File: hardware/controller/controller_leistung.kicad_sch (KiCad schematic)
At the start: 51 parts, among them J1 230V~, J2 LOAD, Q1 AO3401A, Q2 BSS138, Q3 IRLML6346, Q4 IRLML6346, Q5 IRLML6346, U1 IRM-10-5, U2 AP7361C-33E, U7 SN74LVC74AD, U8 TPS3828-33DBV, U9 TC6501P065

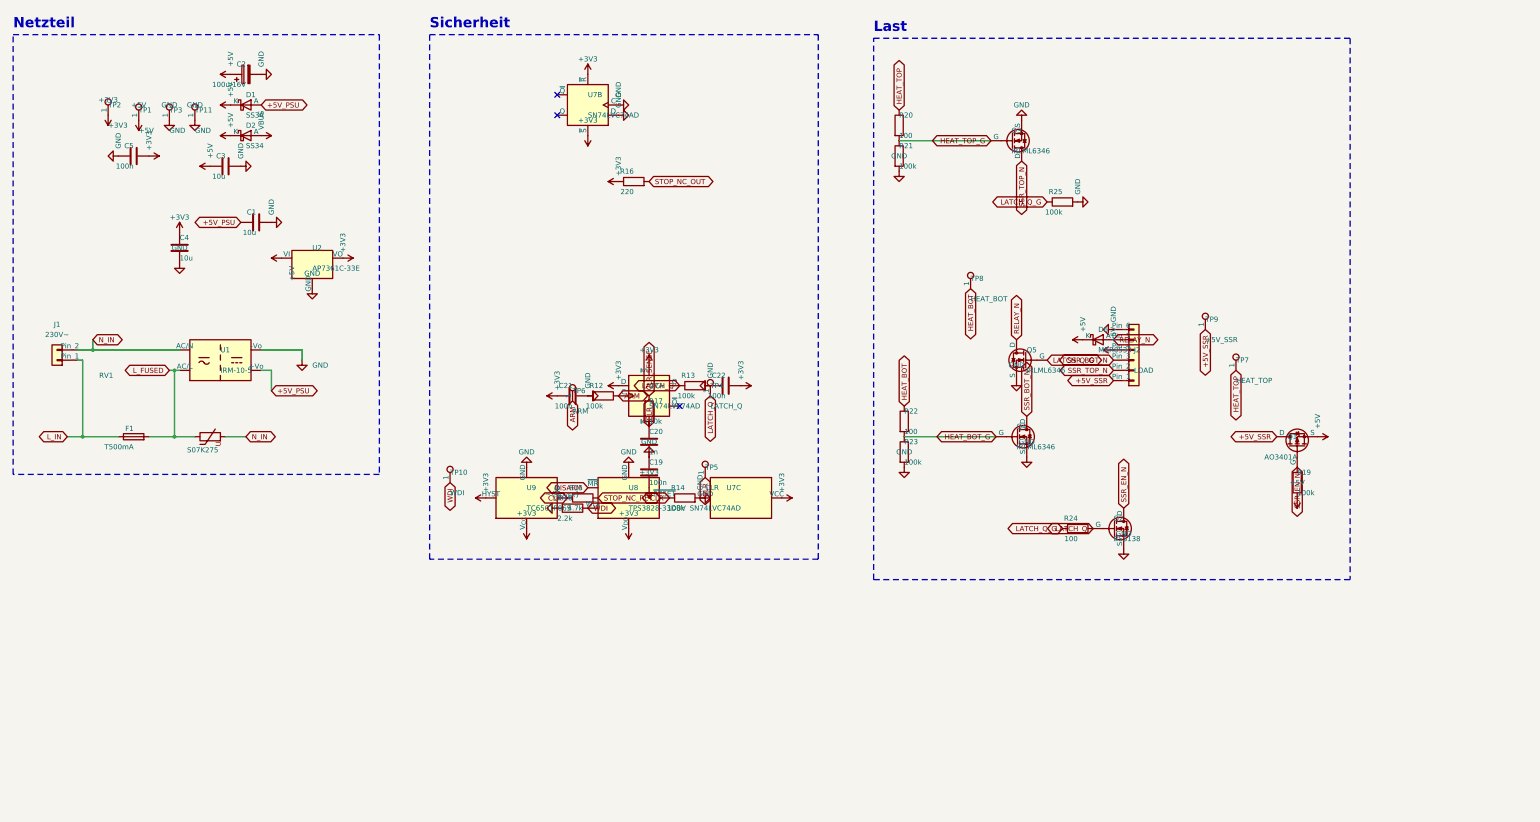
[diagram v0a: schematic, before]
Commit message: feat(hardware): board fan circuit in the schematic (T073), sheet cleanup in progress
Fan header J10 with BSS138 PWM stage (GPIO 38, 1k pull-up to 5 V,
full speed without firmware) and tachometer input (GPIO 37, 10k/1k/1n,
TP12) per research R18. Reference netlist re-exported for this
deliberate change: 129 parts, 73 nets. board_rev_a.h and
check_schematic.py know FAN_TACH/FAN_PWM. PCB updated from the netlist,
new footprints parked below the outline; parity DRC clean.
Includes the user's partial sheet cleanup (T071 still open).

Co-Authored-By: Claude Opus 5.5 <noreply@anthropic.com>
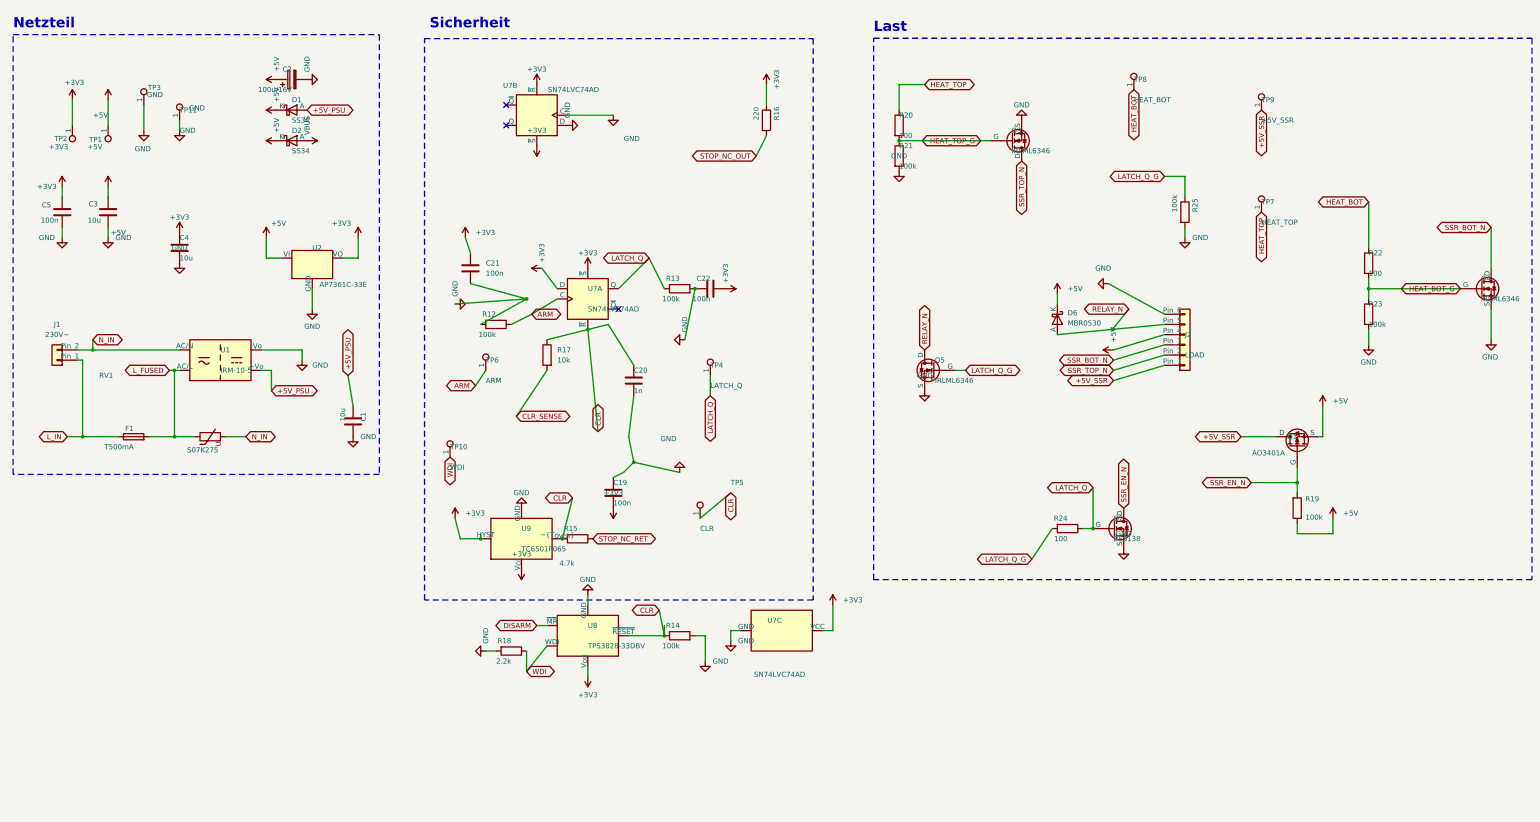
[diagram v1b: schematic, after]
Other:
- moved on the sheet: C1, C19, C2, C20, C21, C22, C3, C5, D1, D2, D6, J2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

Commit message: feat(hardware): sheet cleanup done, ERC clean (T071)
- Leistung/Steuerung sheets cleaned up and readable, intersheet references on
- embedded symbols updated from the libraries (lib_symbol_mismatch gone)
- stray and off-grid wire stubs removed
- PWR_FLAGs on N_IN, L_FUSED, +5V and VBUS
- ERC exclusion for the shared SDO line of U5/U6 (MAX31856, tristate)
- PCB nets re-imported, U7 relinked

kicad-cli ERC: 0 violations, check_schematic: 0 errors, parity DRC clean.

Co-Authored-By: Claude Opus 5.5 <noreply@anthropic.com>
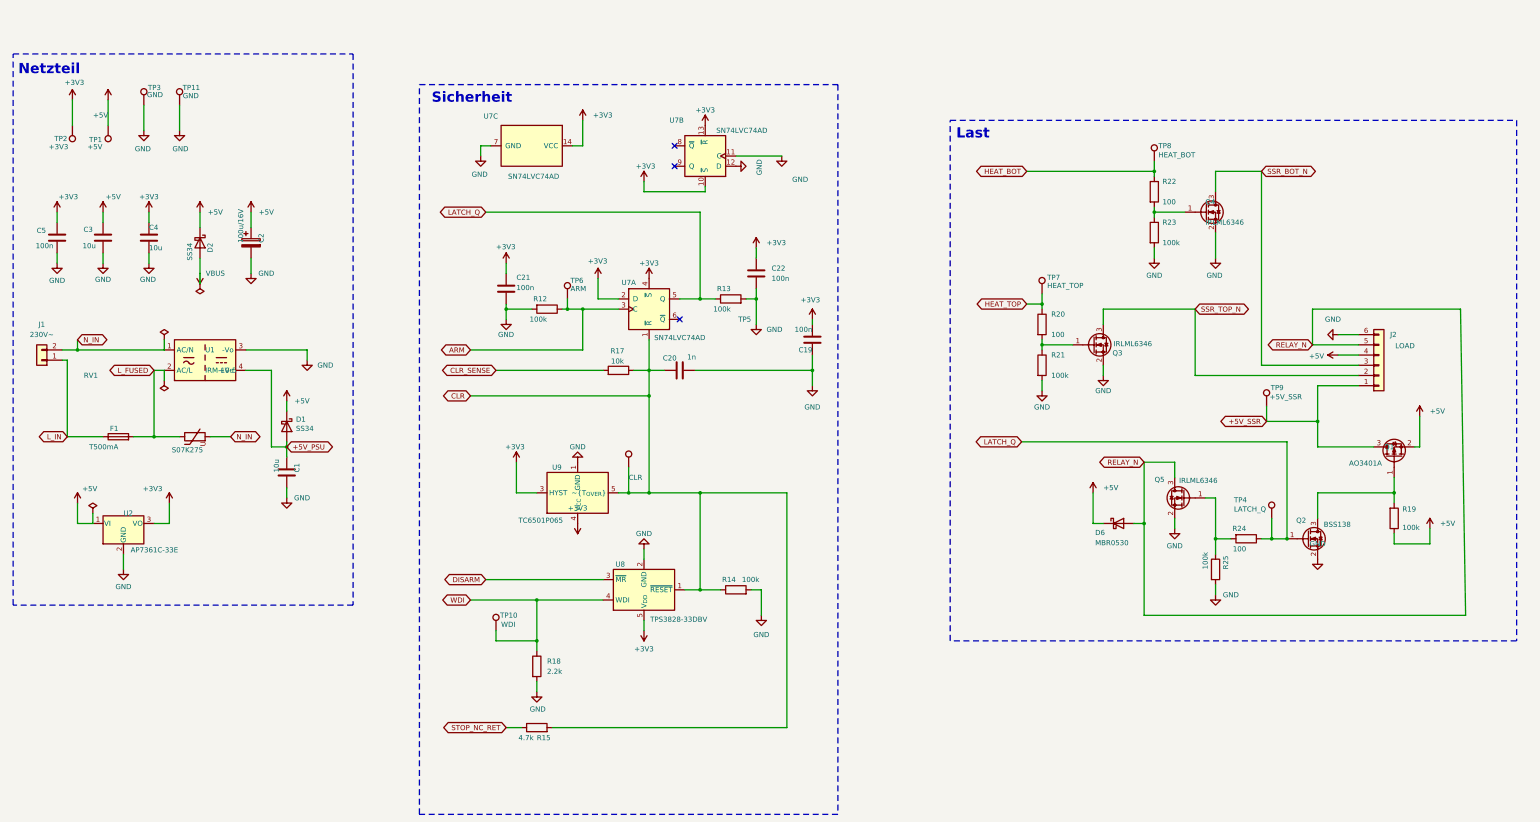
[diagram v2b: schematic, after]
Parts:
- removed R16: 220, Resistor_SMD:R_0603_1608Metric, symbol Device:R
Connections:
- net HEAT_BOT_G: no longer names the net of Q4.1 (G), R22.2, R23.1
- net HEAT_TOP_G: no longer names the net of Q3.1 (G), R20.2, R21.1
- net LATCH_Q_G: no longer names the net of Q5.1 (G), R24.2, R25.1
- net SSR_EN_N: no longer names the net of Q1.1 (G), Q2.3 (D), R19.2
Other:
- moved on the sheet: C1, C19, C2, C20, C21, C22, C3, C4, C5, F1, J1, J2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

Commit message: feat(hardware): thermocouple sockets J5/J6 switched to RS PRO 381-7564
- Omega PCC-SMP-K (46 EUR per 5-pack, dimensions only from an isometric
  drawing) replaced by RS PRO 381-7564 (type K IEC, NiCr/Ni contacts,
  about 5 EUR each, dimensioned drawing in the RS datasheet)
- new footprint oven:RS_381-7564_Horizontal: 2 pins at 7.9 mm, NPTH 2.7 mm
  for an M2.5 screw; polarity still to be checked on a sample
- schematic fields footprint/MPN/source, controller.ref.net re-exported
  (intended change; it also takes over the net names after the label
  cleanup, connectivity unchanged)
- J5/J6 swapped on the board, pins below U5/U6, 2.7 mm gap between them
- small part placement optimised for routing, silkscreen cleaned up (T020)
- value texts at U1/RV1 moved (user)
- docs and BOM updated, old Omega footprint removed

check_schematic: 0 errors, 0 notes; DRC with schematic parity: no
deviation, only unconnected items and 2 silk edge warnings at U1.

Co-Authored-By: Claude Opus 5.5 <noreply@anthropic.com>
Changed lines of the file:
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@@
 		(in_pos_files yes)
 		(dnp no)
-		(fields_autoplaced yes)
 		(property "Reference" "U1"
-			(at 73.66 109.22 0)
+			(at 78.486 105.156 0)
 			(show_name no)
 			(do_not_autoplace no)
@@
 		)
 		(property "Value" "IRM-10-5"
-			(at 73.66 114.3 0)
+			(at 65.024 105.156 0)
 			(show_name no)
 			(do_not_autoplace no)

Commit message: feat(hardware): JST XH connectors, re-placement and re-route, open fuse holder (T087, T021)
Connectors (T087, research R9/R10, contracts/connectors.md):
- J3 display JST XH 1x10 (same pin order as the IDC 2x5)
- J4 encoder JST XH 1x5 (A, GND, B, SW, GND), new J11 stop button
  JST XH 1x4 directly on the main board; an unplugged stop connector
  opens the NC loop like a pressed stop button
- encoder carrier: J1 JST XH 1x5, J2 (stop wires) removed
- schematic wire chains of the old connectors replaced by labels,
  connectivity checked pin by pin; ref netlists re-exported

Layout:
- XH connectors at the right edge, RESET/BOOT moved inside
- decoupling capacitors next to their IC pins (LDO 2.6/2.9 mm,
  MAX31856 2.3-3.7 mm, U7/U8/U9 2.2-4.3 mm, ESP32 5.1 mm)
- EMC: flyback diode D7 at the buzzer, 33 ohm SPI resistors at the
  module pins, C1 on the IRM-10-5 output path, thermal vias at the LDO
- re-routed with Freerouting 1.9.0 (2.5.0 compared and rejected),
  GND stitching and isolated GND groups connected
- manual rework by the user: USB D+/D- through the ESD array U4 at the
  connector, tightly coupled, CC2 connected, U4 pin 2 GND connected
- COV1 restored after an accidental delete, dangling stubs removed
- F1: Schurter OGN 0031.8201 open fuse holder instead of the FAB, whose
  carrier is pulled out axially and was blocked by RV1/IRM-10-5;
  L_FUSED re-routed

DRC with schematic parity: 0 errors, 0 unconnected (2 silk edge
warnings from the U1 footprint); check_schematic 0 errors for both
boards; ERC only the documented SDO exclusion.

Co-Authored-By: Claude Opus 5.5 <noreply@anthropic.com>
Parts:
- F1: footprint Fuse:Fuseholder_Cylinder-5x20mm_Schurter_FAB_0031-355x_Horizontal_Closed -> Fuse:Fuseholder_Cylinder-5x20mm_Schurter_0031_8201_Horizontal_Open; MPN Schurter FAB 0031.355x + 5x20 T500mA -> Schurter OGN 0031.8201 + 5x20 T500mA
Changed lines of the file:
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@@
 			)
 		)
-		(property "Footprint" "Fuse:Fuseholder_Cylinder-5x20mm_Schurter_FAB_0031-355x_Horizontal_Closed"
+		(property "Footprint" "Fuse:Fuseholder_Cylinder-5x20mm_Schurter_0031_8201_Horizontal_Open"
 			(at 52.07 130.81 90)
 			(hide yes)
@@
 			)
 		)
-		(property "MPN" "Schurter FAB 0031.355x + 5x20 T500mA"
+		(property "MPN" "Schurter OGN 0031.8201 + 5x20 T500mA"
 			(at 52.07 135.89 90)
 			(hide yes)

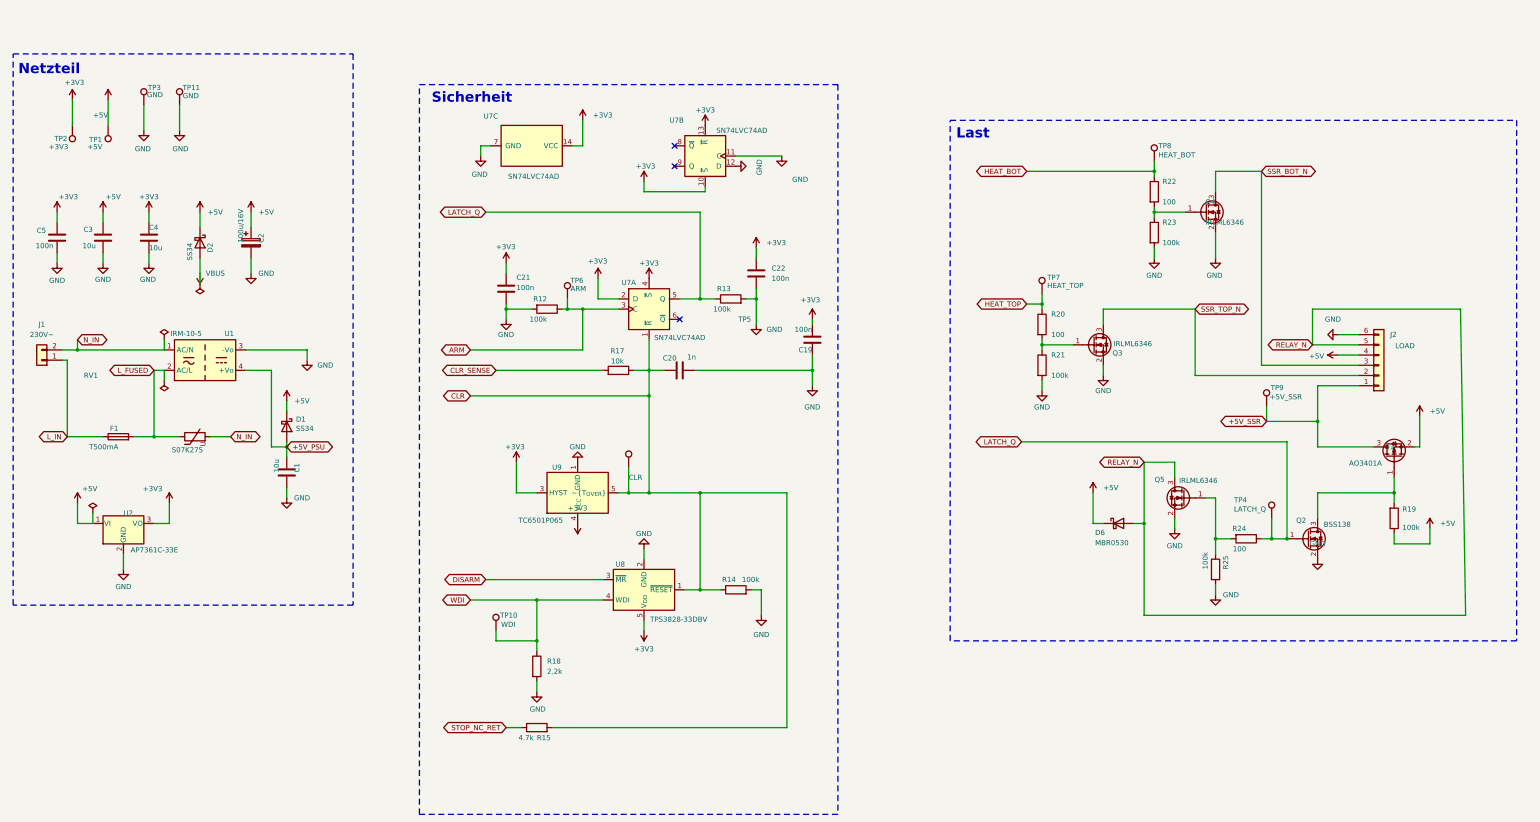
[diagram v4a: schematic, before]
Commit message: feat(hardware): test point groups labelled, TP11 removed, USB shield option R9 DNP
- TP11 (second GND test point) removed, TP1 GND / TP2 3V3 / TP3 5V in a
  new order (user); contracts/connectors.md and controller.ref.net updated
- top silkscreen groups: Versorgung (TP1-3), Freigabe (TP4-6),
  SSR (TP7-9), Last-Relais; test point signal names next to the pads
- small layout optimisations; a GND via under TP4 (short to LATCH_Q) and
  a loose GND via removed, Q3 source re-connected to GND
- USB shield: R9 (0 ohm) marked DNP, shield to GND via R8 1M || C11 4.7n
- editor default pad size in the project file (user)

DRC with schematic parity: 0 errors, 0 unconnected (2 silk edge
warnings from the U1 footprint); GND copper is one connected group;
check_schematic 0 errors for both boards; ERC only the documented SDO
exclusion.

Co-Authored-By: Claude Opus 5.5 <noreply@anthropic.com>
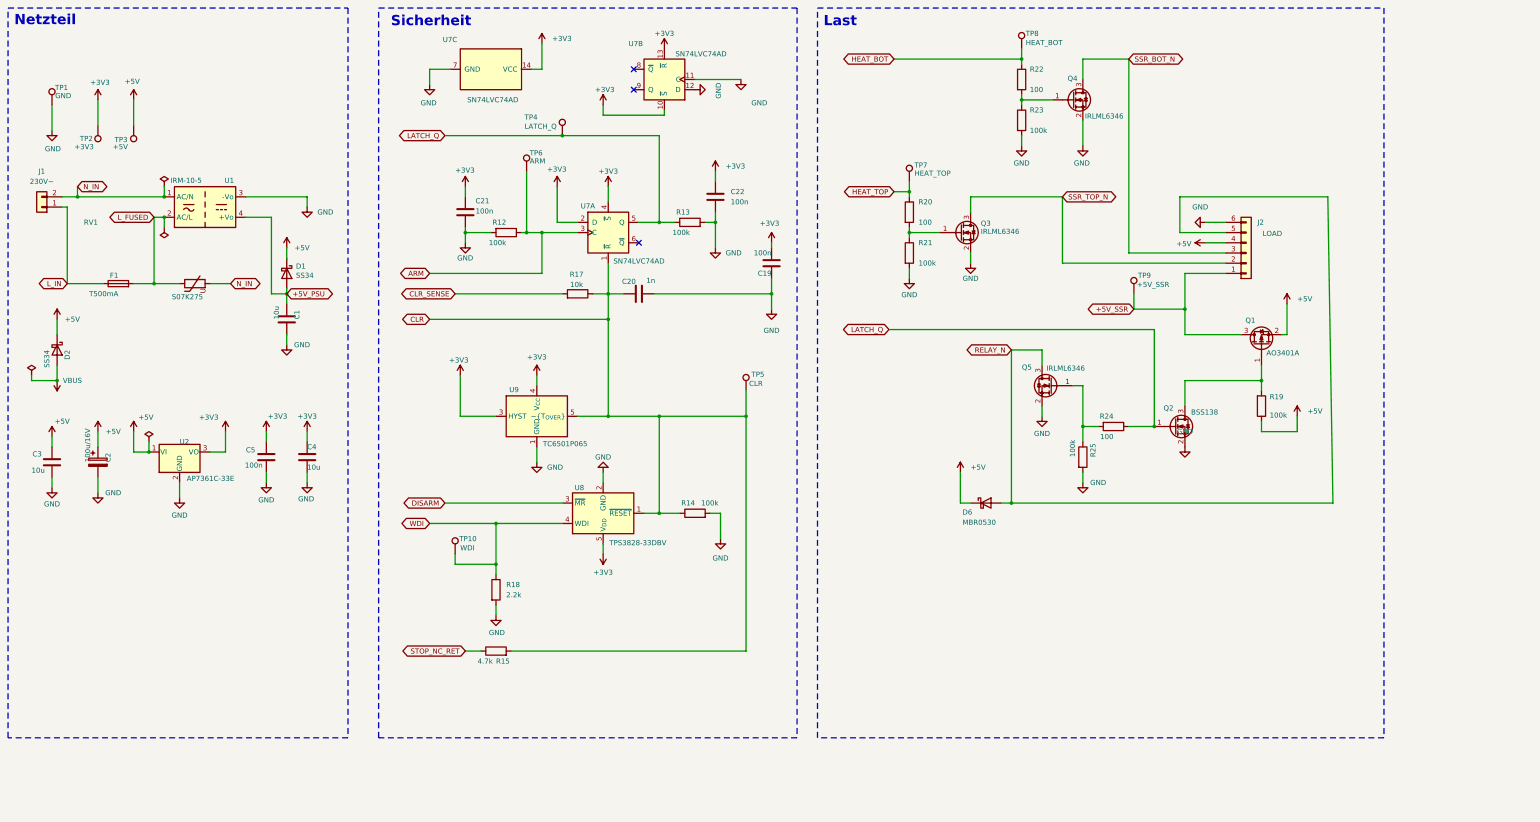
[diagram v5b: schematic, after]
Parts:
- removed TP3: GND, TestPoint:TestPoint_Keystone_5000-5004_Miniature, symbol Connector:TestPoint
- renumbered TP11 to TP1, TP1 to TP3
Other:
- moved on the sheet: C1, C19, C2, C20, C21, C22, C3, C4, C5, D1, D2, D6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

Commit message: feat(hardware): references renumbered, fixed screw terminals J1/J2, 3D models ESP32/IRM-10
- References re-annotated by sheet position; docs, specs, firmware comment,
  check_schematic.py and DRC rule esp32_thermal_vias (U3 -> U9) updated,
  reference netlist re-exported
- Power symbols no longer excluded from simulation
- J1/J2: Phoenix MKDS 1,5/2-5,08 and MKDS 1/6-3,81 instead of pluggable
  MSTBA/MC; own footprints keep the oval pads (3 mm L-N), generated by
  make_terminal_footprints.py
- 3D models for U9 (Espressif) and U2 (Mean Well) in hardware/lib/3dmodels

Co-Authored-By: Claude Opus 5.5 <noreply@anthropic.com>
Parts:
- J1: footprint Connector_Phoenix_MSTB:PhoenixContact_MSTBA_2,5_2-G-5,08_1x02_P5.08mm_Horizontal -> oven:Phoenix_MKDS-1,5-2-5.08_Horizontal_OvalPads; MPN Phoenix MSTBA 2,5/2-G-5,08 + MSTB 2,5/2-ST-5,08 -> Phoenix MKDS 1,5/2-5,08
- J2: footprint Connector_Phoenix_MC:PhoenixContact_MC_1,5_6-G-3.81_1x06_P3.81mm_Horizontal -> oven:Phoenix_MKDS-1-6-3.81_Horizontal_OvalPads; MPN Phoenix MC 1,5/6-G-3,81 + MC 1,5/6-ST-3,81 -> Phoenix MKDS 1/6-3,81
- renumbered C3 to C1, C5 to C3, C1 to C4, C4 to C5, C21 to C6, C20 to C7, C22 to C8, C19 to C9, D2 to D1, D1 to D2, D6 to D3, Q3 to Q1, Q5 to Q2, Q4 to Q3, Q2 to Q4, Q1 to Q5, R18 to R1, R23 to R10, R25 to R11, R24 to R12, R19 to R13, R15 to R2, R12 to R3, R17 to R4, R13 to R5, R14 to R6, R20 to R7, R21 to R8, R22 to R9, TP9 to TP10, TP10 to TP4, TP6 to TP5, TP4 to TP6, TP5 to TP7, TP7 to TP8, TP8 to TP9, U2 to U1, U1 to U2, U7 to U3, U9 to U4, U8 to U5
